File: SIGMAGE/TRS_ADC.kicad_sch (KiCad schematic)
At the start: 30 parts, among them J2 SJ63073E, J3 SJ63073E, U4 OPA1612AIDRGR, U5 PCM1803ADB, U6 OPA1612AIDRGR, U7 PCM1803ADB

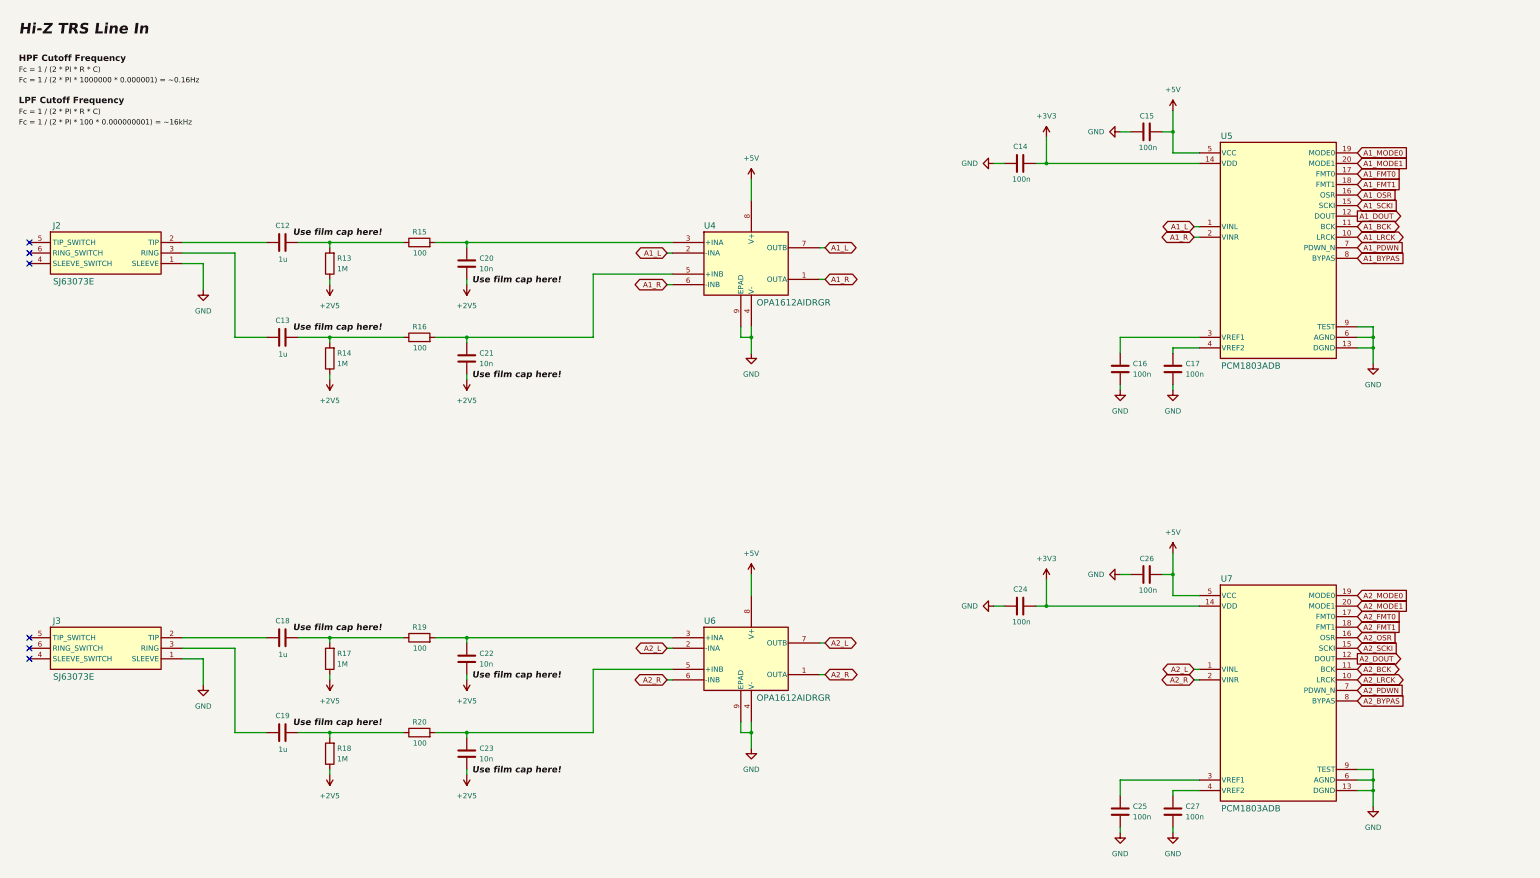
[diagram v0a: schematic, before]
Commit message: Added RJ45/PHY and MCU
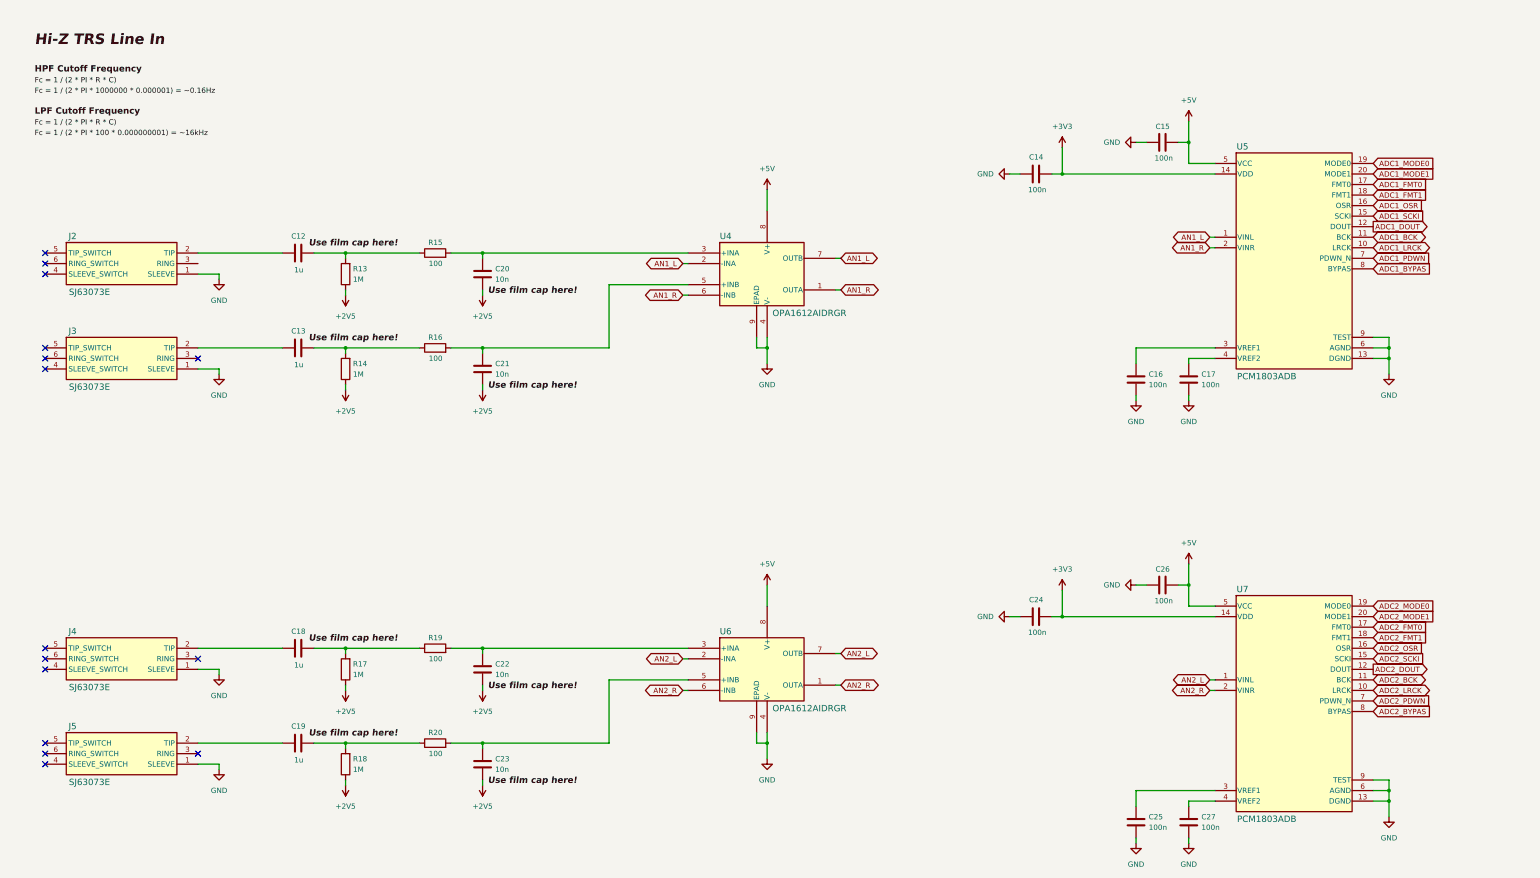
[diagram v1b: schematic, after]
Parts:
- added J4, J5: SJ63073E, SIGMAGE:SJ63073E, symbol SIGMAGE:SJ63073E
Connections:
- net GND: now also J4.1 (SLEEVE), J5.1 (SLEEVE)
- net at C13.1: now also J3.2 (TIP); no longer J2.3 (RING)
- net at C18.1: now also J4.2 (TIP); no longer J3.2 (TIP)
- net at J3.3 (RING): no longer C19.1
- net A1_BCK renamed ADC1_BCK
- net A1_BYPAS renamed ADC1_BYPAS
- net A1_DOUT renamed ADC1_DOUT
- net A1_FMT0 renamed ADC1_FMT0
- net A1_FMT1 renamed ADC1_FMT1
- net A1_L renamed AN1_L
- net A1_LRCK renamed ADC1_LRCK
- net A1_MODE0 renamed ADC1_MODE0
- net A1_MODE1 renamed ADC1_MODE1
- net A1_OSR renamed ADC1_OSR
- net A1_PDWN renamed ADC1_PDWN
- net A1_R renamed AN1_R
- net A1_SCKI renamed ADC1_SCKI
- net A2_BCK renamed ADC2_BCK
- net A2_BYPAS renamed ADC2_BYPAS
- net A2_DOUT renamed ADC2_DOUT
- net A2_FMT0 renamed ADC2_FMT0
- net A2_FMT1 renamed ADC2_FMT1
- net A2_L renamed AN2_L
- net A2_LRCK renamed ADC2_LRCK
- net A2_MODE0 renamed ADC2_MODE0
- net A2_MODE1 renamed ADC2_MODE1
- net A2_OSR renamed ADC2_OSR
- net A2_PDWN renamed ADC2_PDWN
- net A2_R renamed AN2_R
- net A2_SCKI renamed ADC2_SCKI
- new net: C19.1, J5.2 (TIP)
- no-connect marks 6 -> 15
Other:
- moved on the sheet: C12, C13, C14, C15, C16, C17, C18, C19, C20, C21, C22, C23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

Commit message: Finished schematic
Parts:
- added J7, J8: TSW10607GS, SIGMAGE:TSW10607GS, symbol SIGMAGE:TSW10607GS
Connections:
- net +3V3: now also C14.1; no longer C14.2
- net GND: now also C14.2, J7.6, J8.6; no longer C14.1
- net ADC1_FMT0: no longer names the net of U5.17 (FMT0)
- net ADC1_FMT0: now also J7.3
- net ADC1_FMT1: no longer names the net of U5.18 (FMT1)
- net ADC1_FMT1: now also J7.4
- net ADC1_MODE0: no longer names the net of U5.19 (MODE0)
- net ADC1_MODE0: now also J7.1
- net ADC1_MODE1: no longer names the net of U5.20 (MODE1)
- net ADC1_MODE1: now also J7.2
- net ADC1_OSR: no longer names the net of U5.16 (OSR)
- net ADC1_OSR: now also J7.5
- net ADC2_FMT0: no longer names the net of U7.17 (FMT0)
- net ADC2_FMT0: now also J8.3
- net ADC2_FMT1: no longer names the net of U7.18 (FMT1)
- net ADC2_FMT1: now also J8.4
- net ADC2_MODE0: no longer names the net of U7.19 (MODE0)
- net ADC2_MODE0: now also J8.1
- net ADC2_MODE1: no longer names the net of U7.20 (MODE1)
- net ADC2_MODE1: now also J8.2
- net ADC2_OSR: no longer names the net of U7.16 (OSR)
- net ADC2_OSR: now also J8.5
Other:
- moved on the sheet: C12, C13, C14, C15, C16, C17, C18, C19, C20, C21, C22, C23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

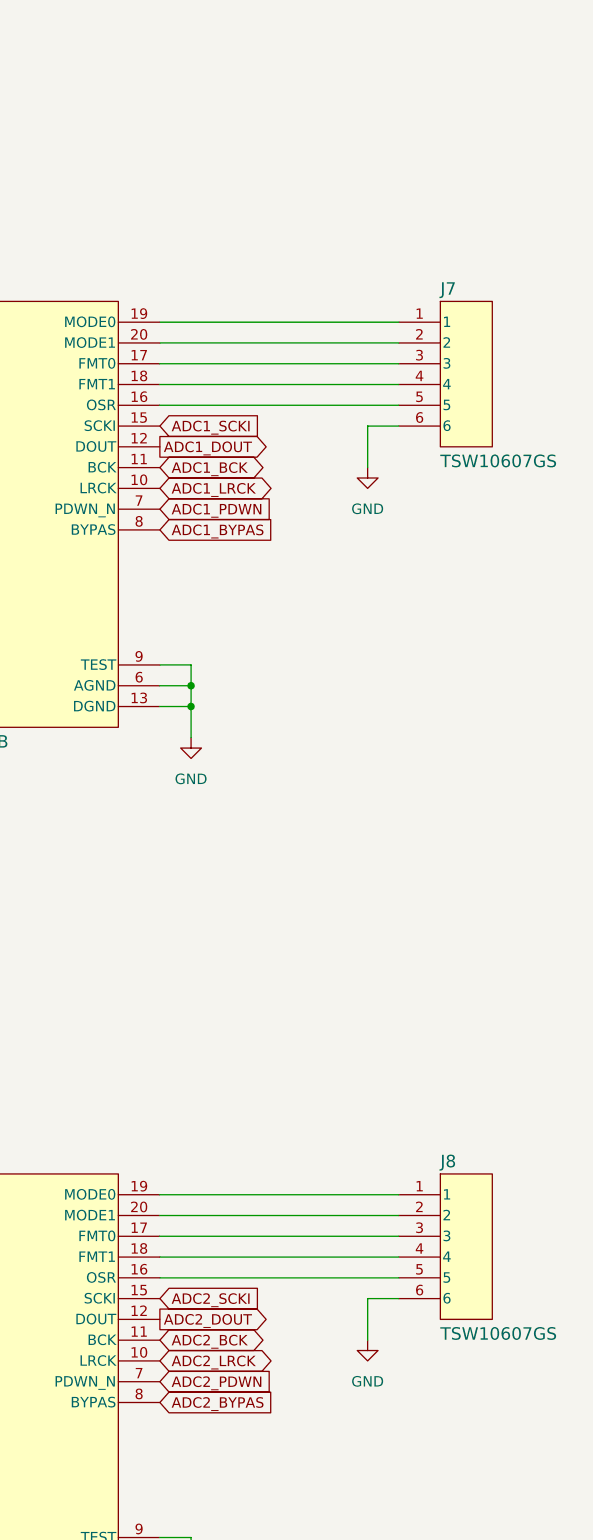
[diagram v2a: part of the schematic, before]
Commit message: Added PCB layout and started routing
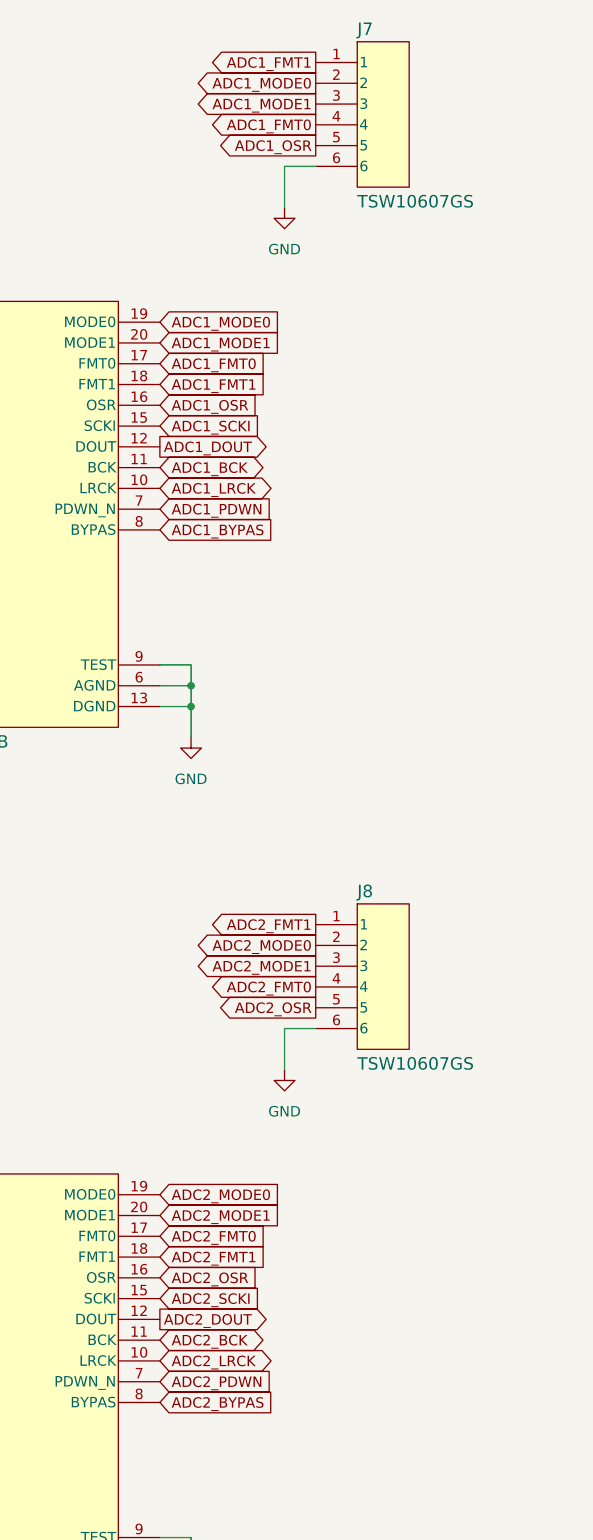
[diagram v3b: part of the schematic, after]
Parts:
- C12, C13, C18, C19, C20, C21, C22, C23: footprint (none) -> Capacitor_SMD:C_1206_3216Metric
- C14, C15, C16, C17, C24, C25, C26, C27: footprint (none) -> Capacitor_SMD:C_0603_1608Metric
- R13, R14, R15, R16, R17, R18, R19, R20: footprint (none) -> Resistor_SMD:R_0603_1608Metric
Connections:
- net ADC2_OSR: now reaches J8.5, U7.16 (OSR)
- net ADC2_FMT0: now reaches U7.17 (FMT0)
- net ADC2_FMT0: now also J8.4; no longer J8.3
- net ADC2_FMT1: now reaches U7.18 (FMT1)
- net ADC2_FMT1: now also J8.1; no longer J8.4
- net ADC2_MODE0: now reaches U7.19 (MODE0)
- net ADC2_MODE0: now also J8.2; no longer J8.1
- net ADC2_MODE1: now reaches U7.20 (MODE1)
- net ADC2_MODE1: now also J8.3; no longer J8.2
- net ADC1_OSR: now reaches J7.5, U5.16 (OSR)
- net ADC1_FMT0: now reaches U5.17 (FMT0)
- net ADC1_FMT0: now also J7.4; no longer J7.3
- net ADC1_FMT1: now reaches U5.18 (FMT1)
- net ADC1_FMT1: now also J7.1; no longer J7.4
- net ADC1_MODE0: now reaches U5.19 (MODE0)
- net ADC1_MODE0: now also J7.2; no longer J7.1
- net ADC1_MODE1: now reaches U5.20 (MODE1)
- net ADC1_MODE1: now also J7.3; no longer J7.2
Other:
- moved on the sheet: J7, J8

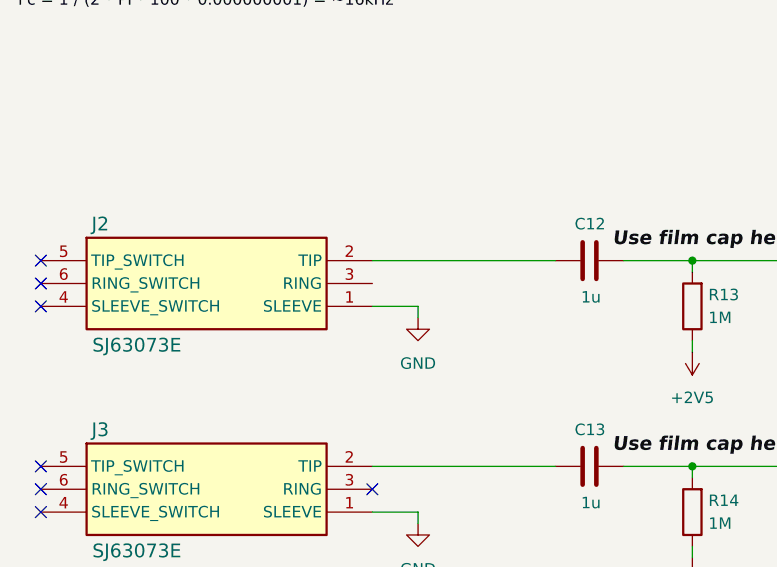
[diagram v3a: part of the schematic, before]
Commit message: Final touches, PCB layout is still horrible, will fix in MK II
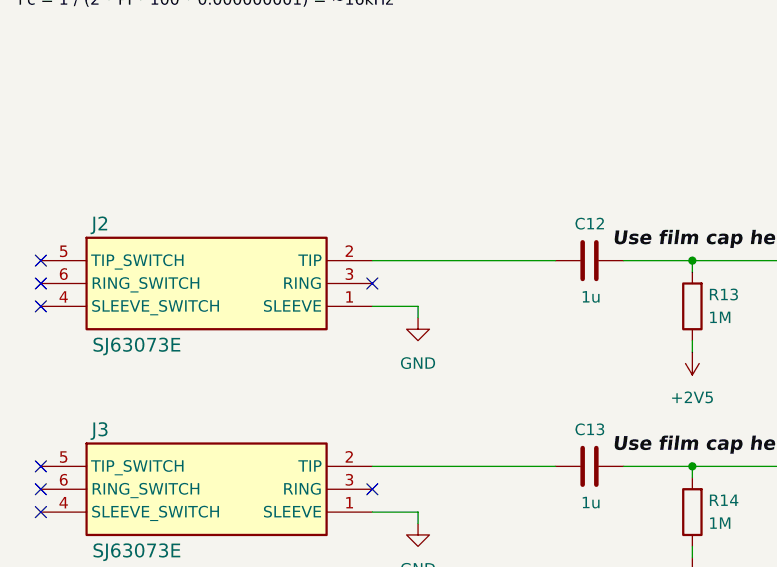
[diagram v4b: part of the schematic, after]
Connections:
- no-connect marks 15 -> 16
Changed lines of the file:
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@@
+	)
+	(no_connect
+		(at 72.39 87.63)
 	)
 	(no_connect
